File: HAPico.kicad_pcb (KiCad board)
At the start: 2 copper layers, 63.5 x 51.5 mm, 30 parts, among them J1 GP 2, J2 GP 3, J3 GP 6, J4 GP 7, J5 GP10, J6 GP11, J7 GP20, J8 GP21, J9 Power Switch, Q1 IRLR024N, Q2 IRLR024N, Q3 IRLR024N, Q4 IRLR024N, Q5 IRLR024N, Q6 IRLR024N, Q7 IRLR024N, Q8 IRLR024N

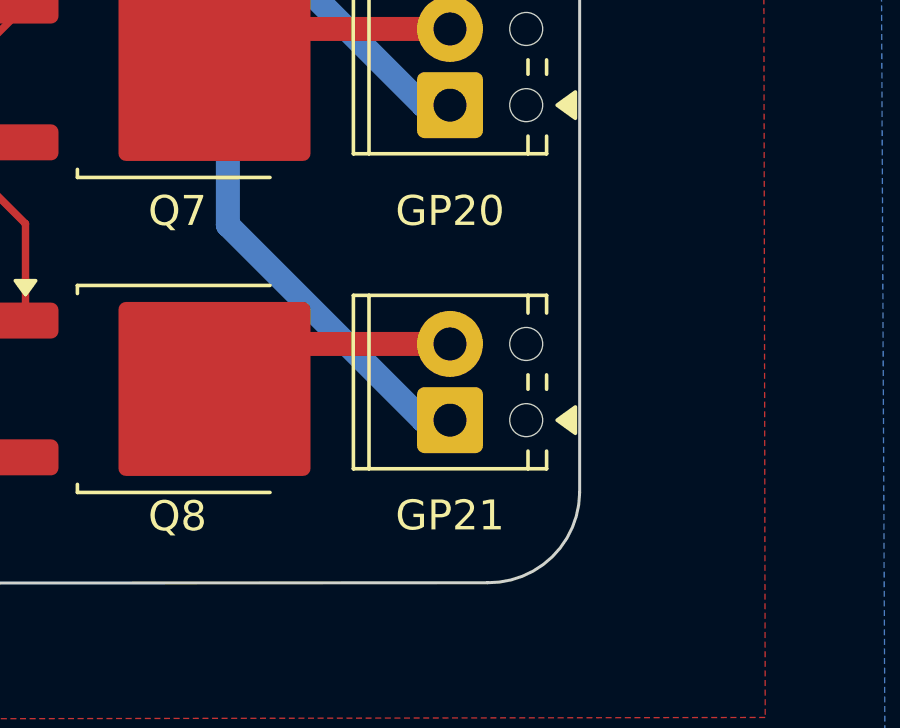
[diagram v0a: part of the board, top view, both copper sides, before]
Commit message: fix: GP20 and 21 were swapped
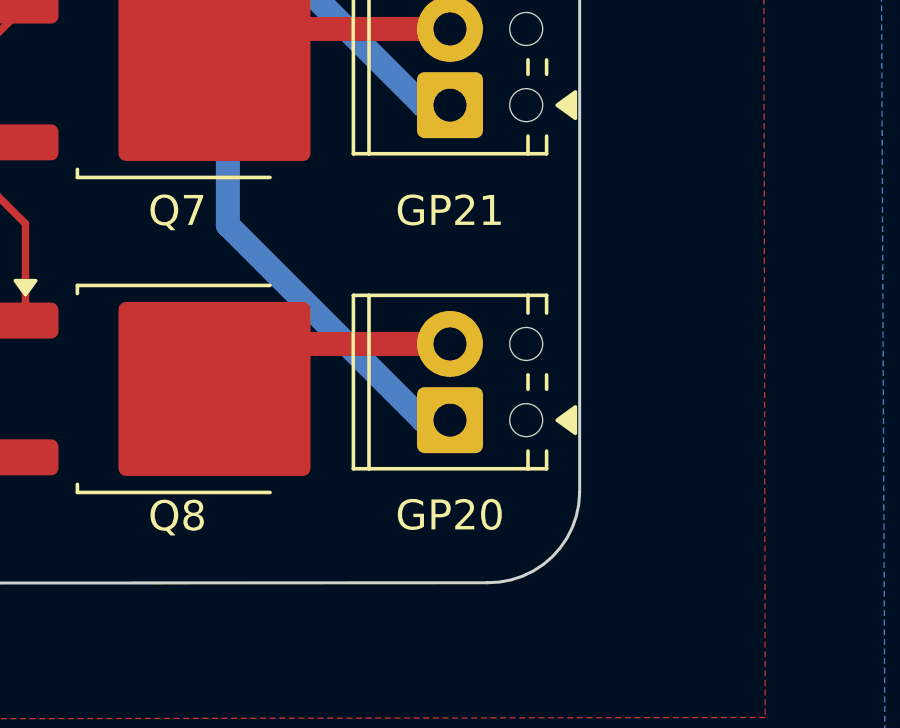
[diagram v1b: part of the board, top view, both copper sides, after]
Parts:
- J7: value GP20 -> GP21
- J8: value GP21 -> GP20
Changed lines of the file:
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@@
 			)
 		)
-		(property "Value" "GP20"
+		(property "Value" "GP21"
 			(at -3.53 0 180)
 			(layer "F.SilkS")
@@
 			)
 		)
-		(property "Value" "GP21"
+		(property "Value" "GP20"
 			(at -3.18 0 180)
 			(layer "F.SilkS")
